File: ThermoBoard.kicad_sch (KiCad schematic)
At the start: 0 parts

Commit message: Extremely incomplete, preliminary, pre-alpha, ugly layout
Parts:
- added H200, H201, H202, H203: MountingHole, MountingHole:MountingHole_3.2mm_M3, symbol Mechanical:MountingHole
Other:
- note added: "Mounting Holes"

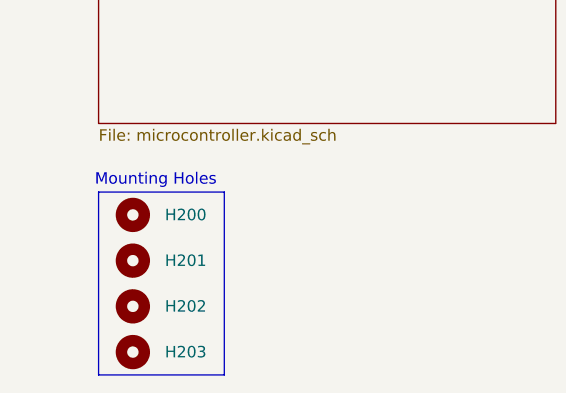
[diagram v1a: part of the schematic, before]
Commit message: First decent layout
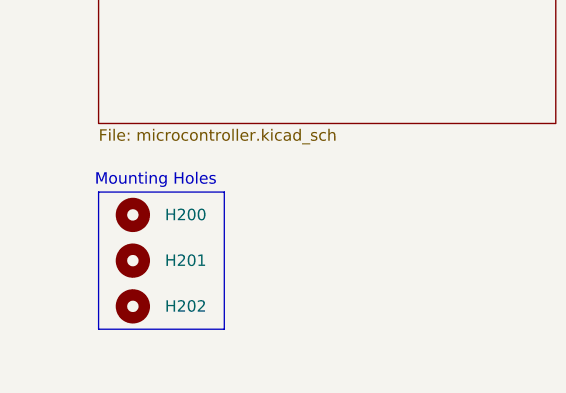
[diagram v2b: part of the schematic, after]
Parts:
- removed H203: MountingHole, MountingHole:MountingHole_3.2mm_M3, symbol Mechanical:MountingHole

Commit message: I hate everything
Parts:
- added H4: MountingHole, MountingHole:MountingHole_3.2mm_M3, symbol Mechanical:MountingHole
- renumbered H200 to H1, H201 to H2, H202 to H3
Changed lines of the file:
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@@
 	(rectangle
 		(start 25.4 167.64)
-		(end 39.37 182.88)
+		(end 39.37 187.96)
 		(stroke
 			(width 0)
@@
 	(symbol
 		(lib_id "Mechanical:MountingHole")
+		(at 29.21 185.42 0)
+		(unit 1)
+		(exclude_from_sim no)
+		(in_bom no)
+		(on_board yes)
+		(dnp no)
+		(property "Reference" "H4"
+			(at 32.766 185.42 0)
+			(effects
+				(font
+					(size 1.27 1.27)
+				)
+				(justify left)
+			)
+		)
+		(property "Value" "MountingHole"
+			(at 31.75 186.6899 0)
+			(effects
+				(font
+					(size 1.27 1.27)
+				)
+				(justify left)
+				(hide yes)
+			)
+		)
+		(property "Footprint" "MountingHole:MountingHole_3.2mm_M3"
+			(at 29.21 185.42 0)
+			(effects
+				(font
+					(size 1.27 1.27)
+				)
+				(hide yes)
+			)
+		)
+		(property "Datasheet" "~"
+			(at 29.21 185.42 0)
+			(effects
+				(font
+					(size 1.27 1.27)
+				)
+				(hide yes)
+			)
+		)
+		(property "Description" "Mounting Hole without connection"
+			(at 29.21 185.42 0)
+			(effects
+				(font
+					(size 1.27 1.27)
+				)
+				(hide yes)
+			)
+		)
+		(instances
+			(project "ThermoBoard"
+				(path "/516571a2-a7c0-4337-8157-ef9156d6d6ba"
+					(reference "H4")
+					(unit 1)
+				)
+			)
+		)
+	)
+	(symbol
+		(lib_id "Mechanical:MountingHole")
 		(at 29.21 170.18 0)
 		(unit 1)
@@
 		(on_board yes)
 		(dnp no)
-		(property "Reference" "H200"
+		(property "Reference" "H1"
 			(at 32.766 170.18 0)
 			(effects
@@
 			(project ""
 				(path "/516571a2-a7c0-4337-8157-ef9156d6d6ba"
-					(reference "H200")
+					(reference "H1")
 					(unit 1)
 				)
@@
 		(on_board yes)
 		(dnp no)
-		(property "Reference" "H201"
+		(property "Reference" "H2"
 			(at 32.766 175.26 0)
 			(effects
@@
 			(project "ThermoBoard"
 				(path "/516571a2-a7c0-4337-8157-ef9156d6d6ba"
-					(reference "H201")
+					(reference "H2")
 					(unit 1)
 				)
@@
 		(on_board yes)
 		(dnp no)
-		(property "Reference" "H202"
+		(property "Reference" "H3"
 			(at 32.766 180.34 0)
 			(effects
@@
 			(project "ThermoBoard"
 				(path "/516571a2-a7c0-4337-8157-ef9156d6d6ba"
-					(reference "H202")
+					(reference "H3")
 					(unit 1)
 				)

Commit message: First workable layout
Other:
- moved on the sheet: H1, H2, H3, H4

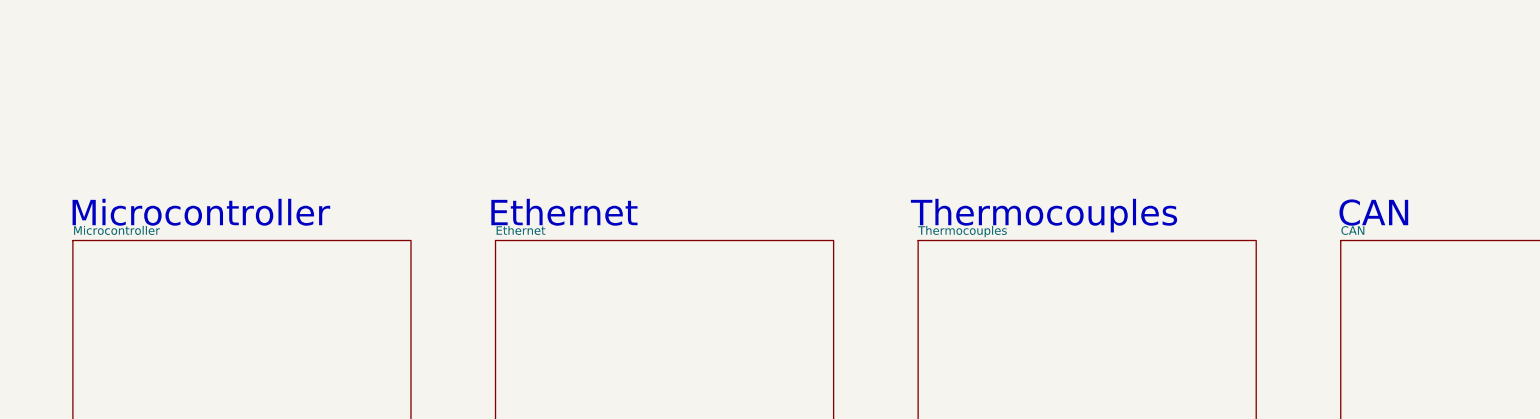
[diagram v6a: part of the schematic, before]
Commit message: Modify repo for usage on Linux, add basic CI
chore: fix CI

Small things
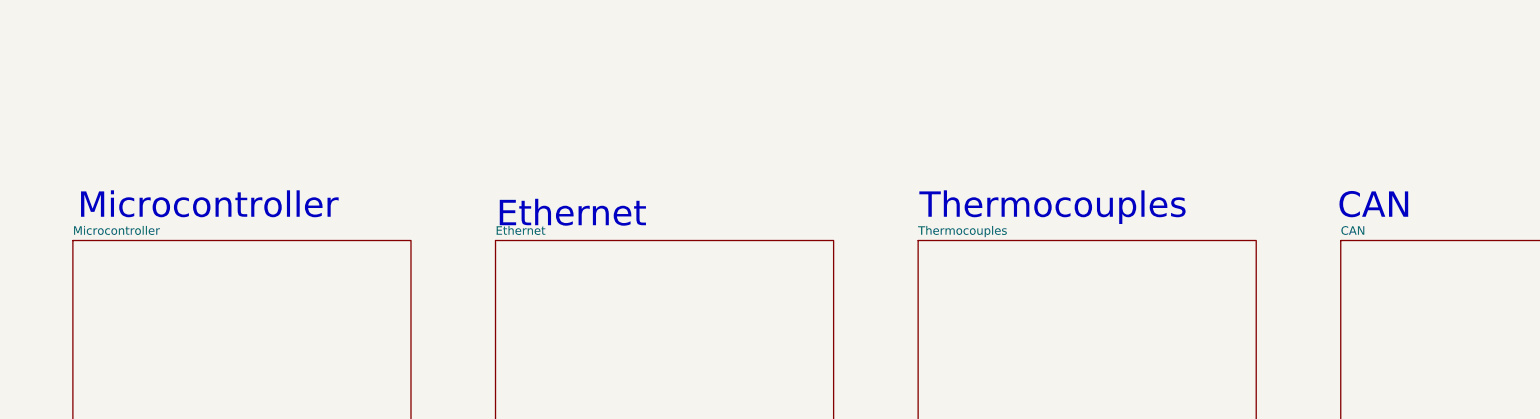
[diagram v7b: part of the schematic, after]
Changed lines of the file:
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@@
 	(text "Thermocouples"
 		(exclude_from_sim no)
-		(at 165.1 127 0)
+		(at 166.37 125.73 0)
 		(effects
 			(font
@@
 	(text "Ethernet"
 		(exclude_from_sim no)
-		(at 92.71 127 0)
+		(at 93.98 127 0)
 		(effects
 			(font
@@
 	(text "Microcontroller"
 		(exclude_from_sim no)
-		(at 38.1 127 0)
+		(at 39.37 125.73 0)
 		(effects
 			(font
@@
 	(text "CAN"
 		(exclude_from_sim no)
-		(at 214.63 127 0)
+		(at 214.63 125.73 0)
 		(effects
 			(font
